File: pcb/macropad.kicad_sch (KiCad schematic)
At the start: 26 parts, among them J1 0.91 OLED display, SW1 SW_Push, SW10 SW_Push, SW11 SW_Push, SW12 SW_Push, SW2 SW_Push, SW3 SW_Push, SW4 SW_Push, SW5 SW_Push, SW6 SW_Push, SW7 SW_Push, SW8 SW_Push, SW9 SW_Push, U1 MOUDLE-SEEEDUINO-XIAO

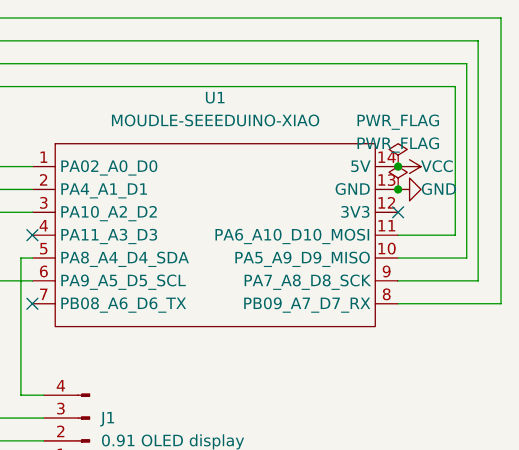
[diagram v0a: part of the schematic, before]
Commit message: Initial commit of cherryblossom pad for Hackpad
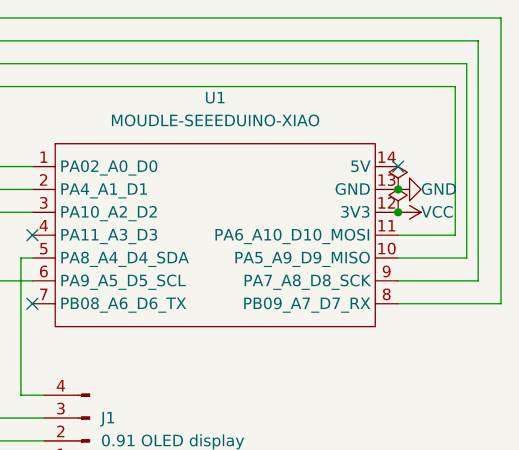
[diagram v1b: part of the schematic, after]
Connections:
- net VCC: now also U1.12 (3V3); no longer U1.14 (5V)
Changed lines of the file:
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@@
   (junction (at 124.46 163.83) (diameter 0) (color 0 0 0 0)
   )
-  (junction (at 222.25 50.8) (diameter 0) (color 0 0 0 0)
-  )
   (junction (at 114.3 105.41) (diameter 0) (color 0 0 0 0)
   )
+  (junction (at 222.25 55.88) (diameter 0) (color 0 0 0 0)
+  )
   (junction (at 124.46 87.63) (diameter 0) (color 0 0 0 0)
   )
@@
   (junction (at 114.3 80.01) (diameter 0) (color 0 0 0 0)
   )
+  (no_connect (at 222.25 50.8))
   (no_connect (at 181.61 66.04))
-  (no_connect (at 222.25 55.88))
   (no_connect (at 181.61 58.42))
   (wire (pts (xy 114.3 80.01) (xy 114.3 105.41))
@@
     )
   )
-  (symbol (lib_id "power:PWR_FLAG") (at 222.25 50.8 0) (unit 1)
-    (in_bom yes) (on_board yes) (dnp no) (fields_autoplaced)
-    (property "Reference" "#FLG01" (at 222.25 48.895 0)
-      (effects (font (size 1.27 1.27)) hide)
-    )
-    (property "Value" "PWR_FLAG" (at 222.25 45.72 0)
-      (effects (font (size 1.27 1.27)))
-    )
-    (property "Footprint" "" (at 222.25 50.8 0)
-      (effects (font (size 1.27 1.27)) hide)
-    )
-    (property "Datasheet" "~" (at 222.25 50.8 0)
-      (effects (font (size 1.27 1.27)) hide)
-    )
-    (pin "1")
-    (instances
-      (project "macropad"
-        (path "/8eb9206d-9a54-423f-b0f0-027a7e59601e"
-          (reference "#FLG01") (unit 1)
-        )
-      )
-    )
-  )
   (symbol (lib_id "Switch:SW_Push") (at 93.98 105.41 0) (unit 1)
     (in_bom yes) (on_board yes) (dnp no) (fields_autoplaced)
@@
     )
   )
+  (symbol (lib_id "power:PWR_FLAG") (at 222.25 55.88 0) (unit 1)
+    (in_bom yes) (on_board yes) (dnp no) (fields_autoplaced)
+    (property "Reference" "#FLG03" (at 222.25 53.975 0)
+      (effects (font (size 1.27 1.27)) hide)
+    )
+    (property "Value" "PWR_FLAG" (at 222.25 50.8 0)
+      (effects (font (size 1.27 1.27)) hide)
+    )
+    (property "Footprint" "" (at 222.25 55.88 0)
+      (effects (font (size 1.27 1.27)) hide)
+    )
+    (property "Datasheet" "~" (at 222.25 55.88 0)
+      (effects (font (size 1.27 1.27)) hide)
+    )
+    (pin "1")
+    (instances
+      (project "macropad"
+        (path "/8eb9206d-9a54-423f-b0f0-027a7e59601e"
+          (reference "#FLG03") (unit 1)
+        )
+      )
+    )
+  )
   (symbol (lib_id "Switch:SW_Push") (at 119.38 105.41 0) (unit 1)
     (in_bom yes) (on_board yes) (dnp no) (fields_autoplaced)
@@
         (path "/8eb9206d-9a54-423f-b0f0-027a7e59601e"
           (reference "SW12") (unit 1)
+        )
+      )
+    )
+  )
+  (symbol (lib_id "power:VCC") (at 222.25 55.88 270) (unit 1)
+    (in_bom yes) (on_board yes) (dnp no)
+    (property "Reference" "#PWR05" (at 218.44 55.88 0)
+      (effects (font (size 1.27 1.27)) hide)
+    )
+    (property "Value" "VCC" (at 224.79 55.88 90)
+      (effects (font (size 1.27 1.27)) (justify left))
+    )
+    (property "Footprint" "" (at 222.25 55.88 0)
+      (effects (font (size 1.27 1.27)) hide)
+    )
+    (property "Datasheet" "" (at 222.25 55.88 0)
+      (effects (font (size 1.27 1.27)) hide)
+    )
+    (pin "1")
+    (instances
+      (project "macropad"
+        (path "/8eb9206d-9a54-423f-b0f0-027a7e59601e"
+          (reference "#PWR05") (unit 1)
         )
       )
@@
     )
     (property "Value" "PWR_FLAG" (at 222.25 48.26 0)
-      (effects (font (size 1.27 1.27)))
+      (effects (font (size 1.27 1.27)) hide)
     )
     (property "Footprint" "" (at 222.25 53.34 0)
@@
         )
       )
-    )
-  )
-  (symbol (lib_id "power:VCC") (at 222.25 50.8 270) (unit 1)
-    (in_bom yes) (on_board yes) (dnp no)
-    (property "Reference" "#PWR01" (at 218.44 50.8 0)
-      (effects (font (size 1.27 1.27)) hide)
-    )
-    (property "Value" "VCC" (at 224.79 50.8 90)
-      (effects (font (size 1.27 1.27)) (justify left))
-    )
-    (property "Footprint" "" (at 222.25 50.8 0)
-      (effects (font (size 1.27 1.27)) hide)
-    )
-    (property "Datasheet" "" (at 222.25 50.8 0)
-      (effects (font (size 1.27 1.27)) hide)
-    )
-    (pin "1")
-    (instances
-      (project "macropad"
-        (path "/8eb9206d-9a54-423f-b0f0-027a7e59601e"
-          (reference "#PWR01") (unit 1)
-        )
-      )
